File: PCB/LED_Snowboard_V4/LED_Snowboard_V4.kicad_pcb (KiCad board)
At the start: 4 copper layers, 100 x 100 mm, 114 parts, among them J1 Charge_Balance, J10 Output, J11 Micro_SD_Card_Det_Hirose_DM3AT, J12 Power Switch, J2 Bat2_Balance, J3 Bat1_Balance, J4 Bat1, J5 Bat2, J7 LED Data, J8 Sensor Input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

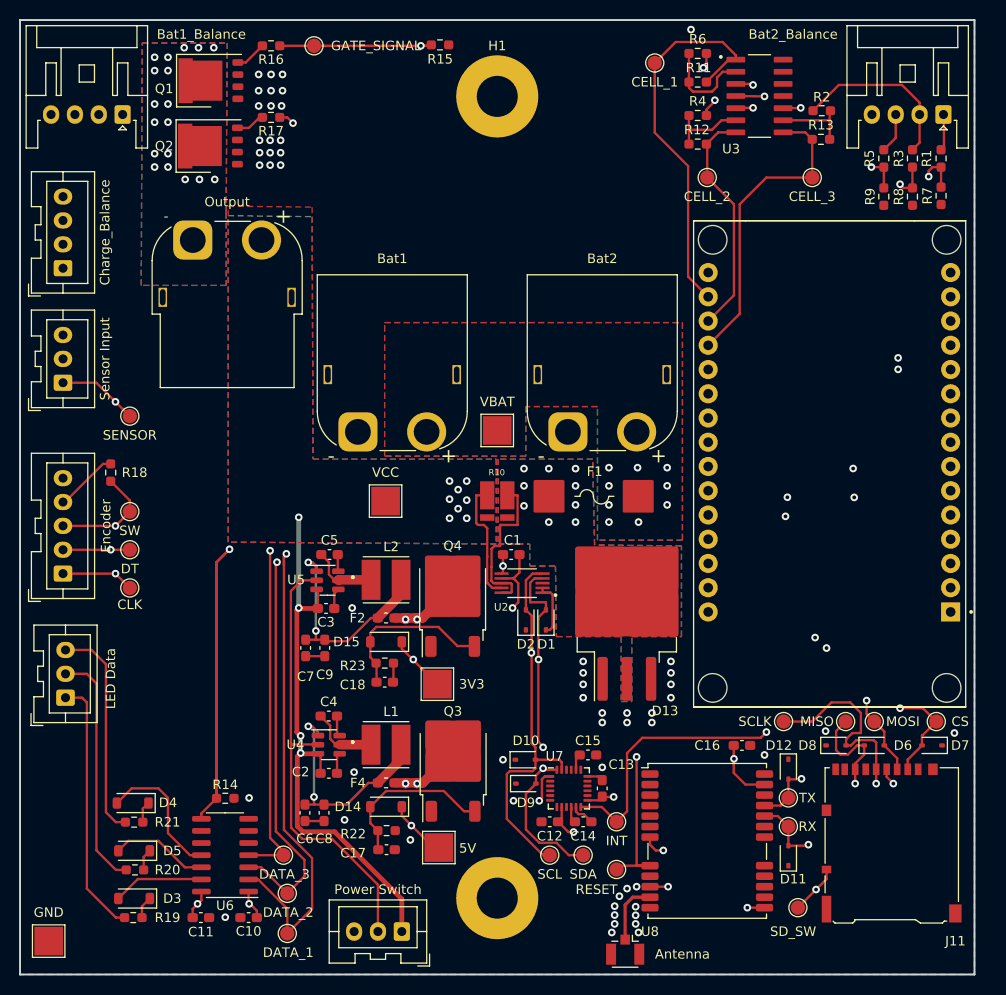
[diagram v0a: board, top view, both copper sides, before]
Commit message: Added Ram
Added Ram. need to finish DRC checks
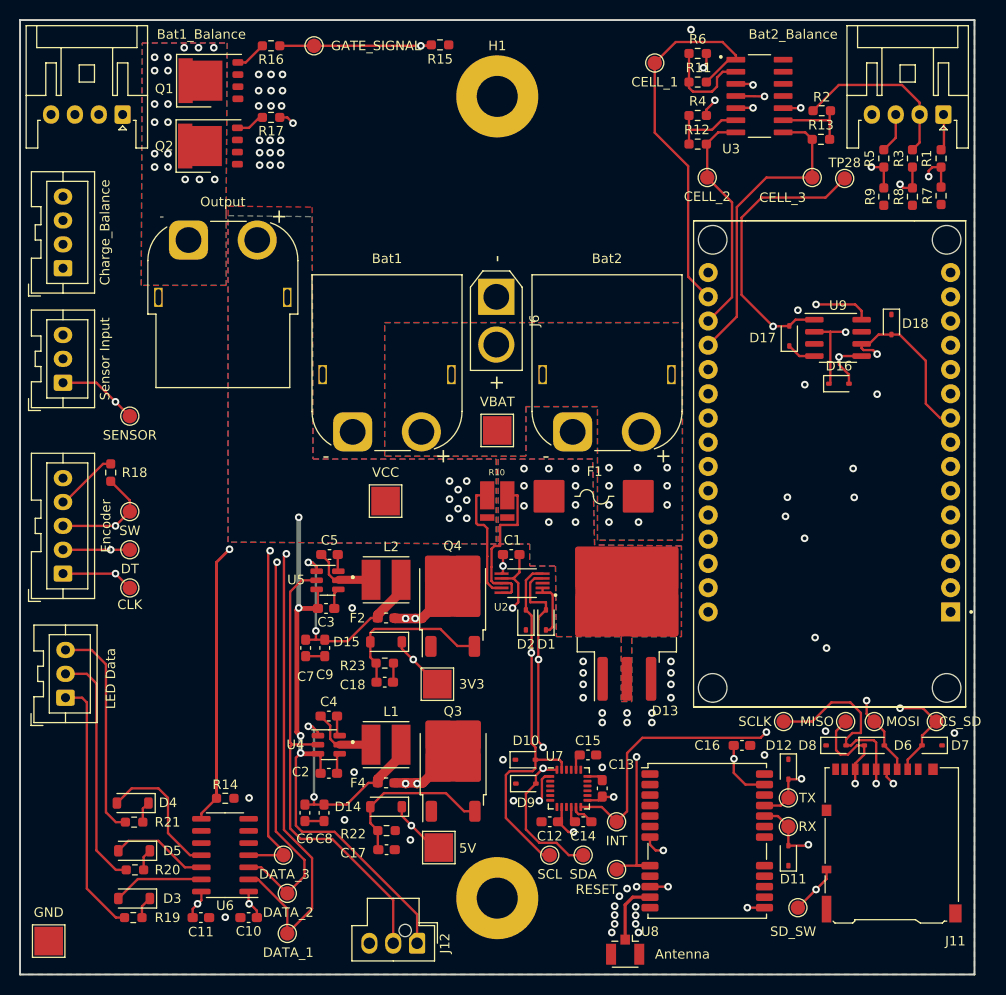
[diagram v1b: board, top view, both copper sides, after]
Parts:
- added D16: SD05_SOD323, Diode_SMD:D_SOD-323, F.Cu at (185.8, 88.1)
- added D17: SD05_SOD323, Diode_SMD:D_SOD-323, F.Cu at (180.6, 83.1)
- added D18: SD05_SOD323, Diode_SMD:D_SOD-323, F.Cu at (191.3, 81.9)
- added J6: ~, Connector_AMASS:AMASS_XT30U-M_1x02_P5.0mm_Vertical, F.Cu at (149.9, 79.0)
- added TP28: CS_RAM, TestPoint:TestPoint_Pad_D1.5mm, F.Cu at (186.4, 66.6)
- added U9: ESP-PSRAM32, Package_SO:SOIC-8_3.9x4.9mm_P1.27mm, F.Cu at (185.7, 83.3)
- J12: footprint Connector_JST:JST_XA_B03B-XASK-1_1x03_P2.50mm_Vertical -> Connector_Molex:Molex_Nano-Fit_105309-xx03_1x03_P2.50mm_Vertical
- TP13: value CS -> CS_SD
- moved J12 2.02 mm to (141.6, 146.7), turned to -90 degrees
- moved J4 0.55 mm to (134.8, 93.2)
- moved J5 0.50 mm to (157.9, 93.2)
- moved J10 0.45 mm to (117.7, 73.0)
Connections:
- net /esp32/CS renamed /esp32/CS_SD
- AE1 pad 2: GND -> (no net)
- U1 pad 27: unconnected-(U1-G2-Pad27) -> /esp32/CS_RAM
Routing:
- net /esp32/CS_RAM: track 0.00 -> 68.8 mm, vias 0 -> 2
- net /esp32/SCLK: track 63.3 -> 86.1 mm, vias 1 -> 2
- net /esp32/MISO: track 56.6 -> 77.4 mm, vias 1 -> 3
- net /esp32/MOSI: track 57.1 -> 70.8 mm, vias 1 -> 2
- net /IO and Power/SCL: track 113.9 -> 122.6 mm
- net /IO and Power/SENSOR: track 72.0 -> 79.2 mm
- net /IO and Power/SDA: track 107.6 -> 114.3 mm
- net +3V3: track 44.0 -> 49.7 mm, vias 11 -> 12
- net GND: track 37.3 -> 40.3 mm
- net VCC: track 71.2 -> 73.3 mm
- net Net-(J12-Pin_2): track 47.5 -> 49.4 mm
- net /IO and Power/DATA_1: track 95.9 -> 94.9 mm

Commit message: Finished PCB with all feedback
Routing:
- net GND: track 40.3 -> 46.2 mm

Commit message: updated control pcb
updated to add high side switching as well as added voltage divider and adjusted layout
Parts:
- removed D1, D10, D11, D12, D16, D17, D18, D2: SD05_SOD323, Diode_SMD:D_SOD-323
- removed D14, D15: D_Zener, Diode_SMD:D_SOD-123
- removed D3, D4, D5: D_Schottky, Diode_SMD:D_SOD-123
- removed F2, F4: Fuse, Fuse:Fuse_0603_1608Metric_Pad1.05x0.95mm_HandSolder
- removed Q3, Q4: X0202NN, Package_TO_SOT_SMD:TO-252-2
- removed R23: 1k, Resistor_SMD:R_0603_1608Metric_Pad0.98x0.95mm_HandSolder
- added C19: .1uF, Capacitor_SMD:C_0603_1608Metric_Pad1.08x0.95mm_HandSolder, F.Cu at (136.7, 108.9)
- added C20: .1uF, Capacitor_SMD:C_0603_1608Metric_Pad1.08x0.95mm_HandSolder, F.Cu at (194.7, 107.8)
- added C21: 0.1uF, Capacitor_SMD:C_0603_1608Metric_Pad1.08x0.95mm_HandSolder, F.Cu at (187.3, 79.6)
- added C22: 0.1uF, Capacitor_SMD:C_0603_1608Metric_Pad1.08x0.95mm_HandSolder, F.Cu at (182.5, 128.8)
- added TP29: BAT, TestPoint:TestPoint_Pad_D1.5mm, F.Cu at (146.8, 116.4)
- added U10: 1EDL8011XUMA1, footprints:PG-DSO-8-92_INF, F.Cu at (137.0, 113.6)
- C10, C11: value C -> .1uF
- C17: value .1uF -> 10uF
- C18: value .1uF -> 10n
- F1: value Fuse -> 35A Fuse
- L1: value 4.7uF -> 4.7uH
- L2: value 3.9uF -> 3.9uH
- Q1, Q2: value ~ -> IRFH5300TRPBF
- R15: value 10k -> 422k
- R16: value 1k -> 100
- R17: value 1k -> 500k
- R22: value 1k -> 100k
- TP13: value CS_SD -> CS
- moved TP5 86.3 mm to (117.7, 61.5)
- moved TP6 66.4 mm to (132.4, 119.1)
- moved R16 66.2 mm to (140.9, 117.3), turned to -90 degrees
- moved R15 59.3 mm to (141.0, 111.8), turned to -90 degrees
- moved R17 53.9 mm to (146.8, 110.1), turned to 90 degrees
- moved Q1 47.3 mm to (140.2, 99.1), turned to 0 degrees
- moved Q2 46.5 mm to (140.2, 105.0), turned to 0 degrees
- moved D9 34.8 mm to (187.5, 125.6), turned to -90 degrees
- moved C17 25.8 mm to (133.0, 111.7), turned to 90 degrees
- moved R22 24.0 mm to (147.7, 112.8)
- moved TP14 22.6 mm to (152.6, 115.1)
- moved TP15 21.8 mm to (156.2, 115.9)
- moved R19 19.5 mm to (104.4, 126.0), turned to -90 degrees
- moved TP7 17.8 mm to (111.3, 139.6)
- moved TP8 17.3 mm to (111.3, 137.0)
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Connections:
- C17 pad 2: Net-(D14-A) -> VCC
- C18 pad 1: GND -> Net-(U10-CFN)
- C18 pad 2: Net-(D15-A) -> Net-(C18-Pad2)
- C6 pad 2: Net-(U4-FB) -> +5V
- C7 pad 2: Net-(U5-FB) -> +3V3
- C8 pad 2: Net-(U4-FB) -> +5V
- C9 pad 2: Net-(U5-FB) -> +3V3
- D6 pad 1: /esp32/MISO -> GND
- D9 pad 2: /IO and Power/SDA -> /esp32/MISO
- J10 pad 1: Net-(Q1-D) -> GND
- J10 pad 2: VCC -> Net-(Q1-S)
- L1 pad 2: Net-(U4-FB) -> +5V
- L2 pad 2: Net-(U5-FB) -> +3V3
- Q1 pad 1: GND -> Net-(Q1-S)
- Q1 pad 3: Net-(Q1-D) -> VCC
- Q2 pad 1: GND -> Net-(Q1-S)
- Q2 pad 2: Net-(Q2-G) -> Net-(Q1-G)
- Q2 pad 3: Net-(Q1-D) -> VCC
- R15 pad 1: /IO and Power/GATE_SIGNAL -> Net-(U10-ILIMIT)
- R16 pad 1: /IO and Power/GATE_SIGNAL -> Net-(U10-CFP)
- R16 pad 2: Net-(Q1-G) -> Net-(C18-Pad2)
- R17 pad 1: /IO and Power/GATE_SIGNAL -> /IO and Power/BAT
- R17 pad 2: Net-(Q2-G) -> VCC
- R19 pad 2: Net-(D3-K) -> Net-(U6-B1)
- R20 pad 2: Net-(D5-K) -> Net-(U6-B2)
- R21 pad 2: Net-(D4-K) -> Net-(U6-B3)
- R22 pad 1: Net-(D14-A) -> /IO and Power/BAT
- U1 pad 28: unconnected-(U1-G15-Pad28) -> /IO and Power/BAT
- U4 pad 1: Net-(U4-FB) -> +5V
- U5 pad 1: Net-(U5-FB) -> +3V3
- U6 pad 11: Net-(D4-A) -> Net-(U6-B3)
- U6 pad 12: Net-(D5-A) -> Net-(U6-B2)
- U6 pad 13: Net-(D3-A) -> Net-(U6-B1)
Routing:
- net /IO and Power/GATE_SIGNAL: track 226.0 -> 114.6 mm, vias 4 -> 3
- net /IO and Power/BAT: track 0.00 -> 61.9 mm, vias 0 -> 1
- net GND: track 46.2 -> 102.4 mm, vias 60 -> 44
- net +3V3: track 49.3 -> 15.5 mm, vias 12 -> 0
- net /esp32/SCLK: track 86.1 -> 59.2 mm, vias 2 -> 3
- net Net-(U4-FB): track 23.9 -> 0.00 mm, vias 2 -> 0
- net Net-(U5-FB): track 23.9 -> 0.00 mm, vias 2 -> 0
- net Net-(J7-Pin_1): track 27.2 -> 4.29 mm
- net Net-(J12-Pin_2): track 49.4 -> 27.8 mm, vias 0 -> 2
- net /IO and Power/SDA: track 114.5 -> 96.3 mm, vias 5 -> 4
- net Net-(J7-Pin_2): track 25.1 -> 7.20 mm
- net Net-(D15-A): track 17.3 -> 0.00 mm
- net Net-(D14-A): track 17.2 -> 0.00 mm
- net /esp32/MISO: track 77.4 -> 62.2 mm
- net Net-(U6-B1): track 0.00 -> 14.9 mm
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- added copper zone on F.Cu, net +3V3
- added copper zone on F.Cu, net +5V
- added copper zone on B.Cu, net Net-(Q1-S)
- added copper zone on F.Cu, net Net-(Q1-S)
- removed copper zone on In1.Cu, net +3V3
- removed copper zone on In1.Cu, net +5V
- removed copper zone on B.Cu, net Net-(Q1-D)
- removed copper zone on F.Cu, net Net-(Q1-D)
- removed copper zone on B.Cu, net VCC
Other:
- board text added: "BAT"
- board text added: "CS_RAM"
